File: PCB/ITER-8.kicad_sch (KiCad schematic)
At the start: 23 parts, among them J1 DC-005, J2 Conn_01x16, J3 Conn_01x08, J4 Conn_01x02, SW1 A11JP, SW2 Dual Push Button, U1 W65C02S6TPG-14, U2 AT28C256-15PU, U3 AS6C62256-55PCN, U4 W65C22SxP, U5 SN74HC00N, Y1 ECS-100AX-010

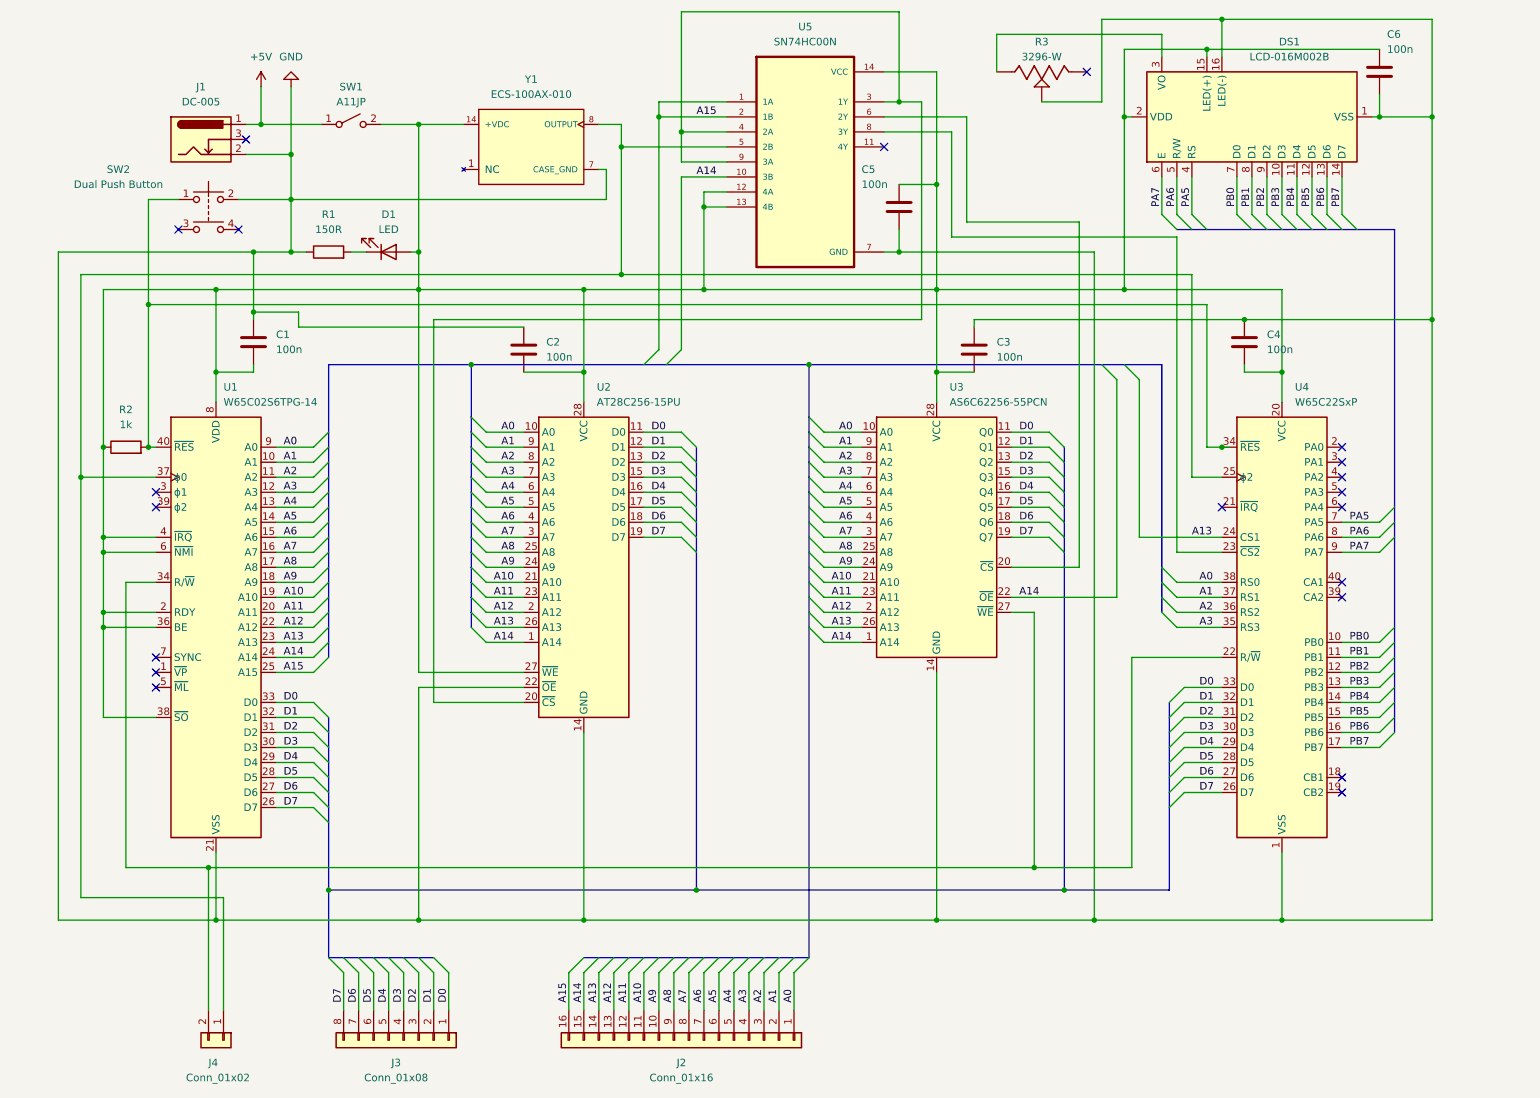
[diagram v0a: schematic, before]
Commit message: 4-bit LCD
LCD in 4-bit mode, including assembly subroutines for timings. New test of the division with remainder.
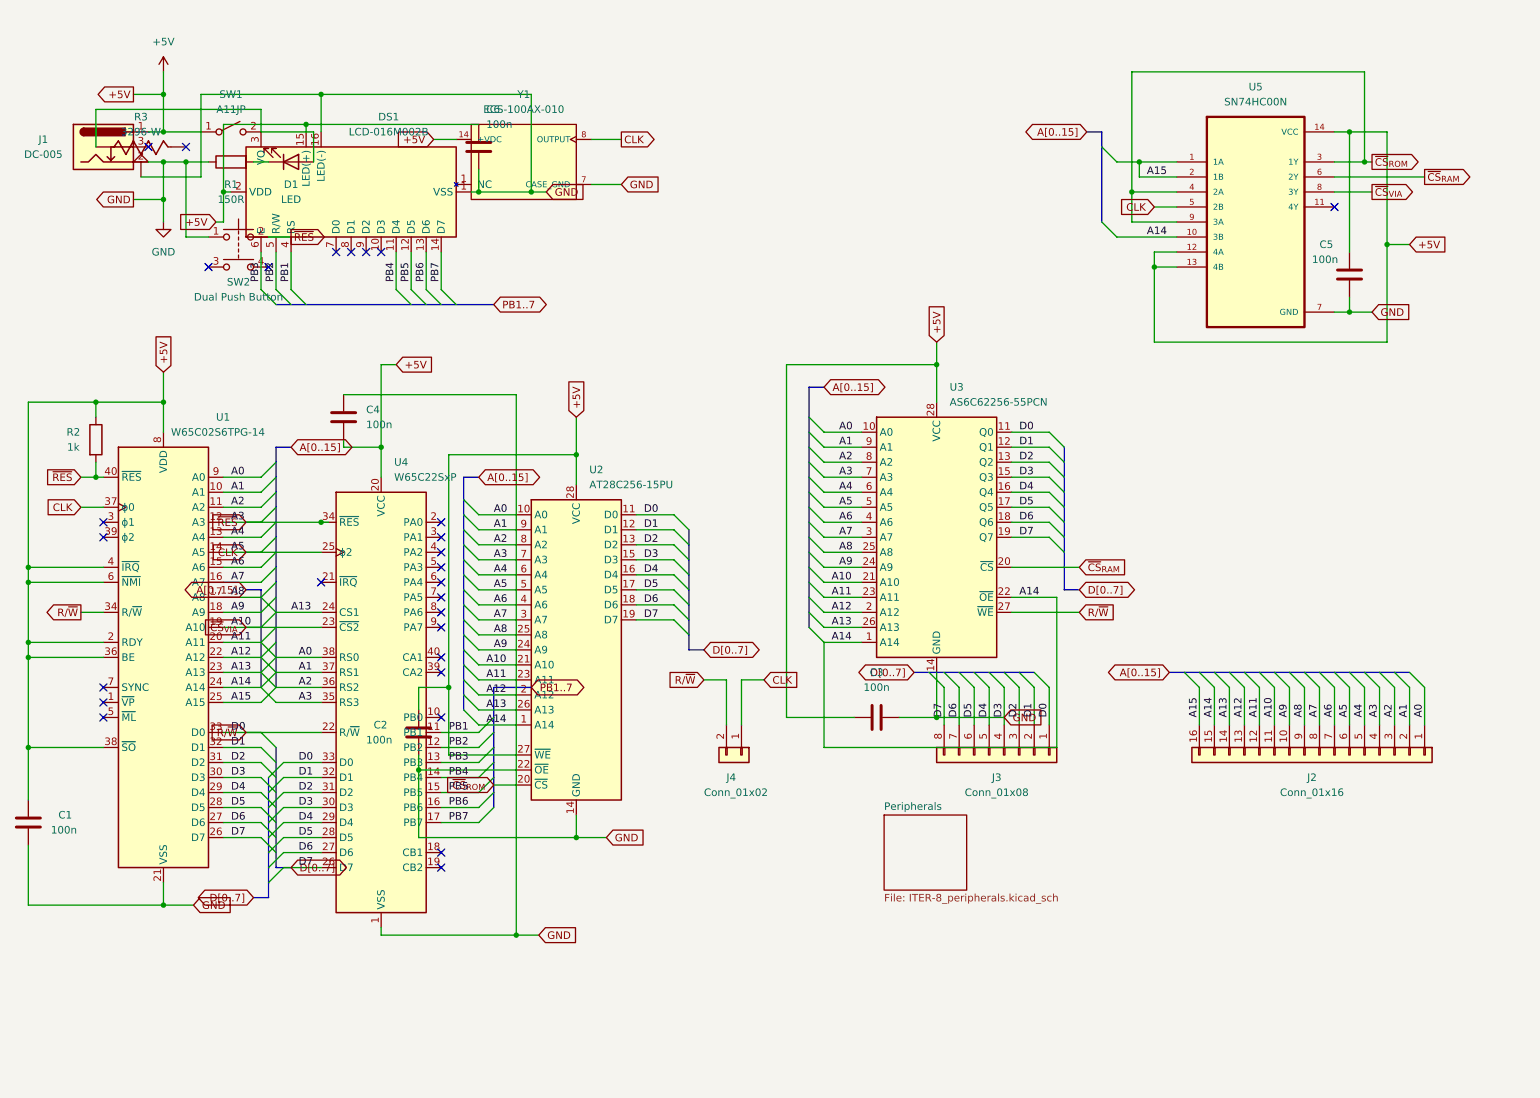
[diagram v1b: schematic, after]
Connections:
- net A10 is gone; now on net ~{CS}_{VIA}: J2.11 (Pin_11), U1.19 (A10), U2.21 (A10), U3.21 (A10)
- net A3 is gone; now on net ~{RES}: J2.4 (Pin_4), U1.12 (A3), U2.7 (A3), U3.7 (A3), U4.35 (RS3)
- net A5 is gone; now on net CLK: J2.6 (Pin_6), U1.14 (A5), U2.5 (A5), U3.5 (A5)
- net D0 is gone; now on net R/~{W}: J3.1 (Pin_1), U1.33 (D0), U2.11 (D0), U3.11 (Q0), U4.33 (D0)
- net D3 is gone; now on net GND: J3.4 (Pin_4), U1.30 (D3), U2.15 (D3), U3.15 (Q3), U4.30 (D3)
- net D4 is gone; now on net GND: J3.5 (Pin_5), U1.29 (D4), U2.16 (D4), U3.16 (Q4), U4.29 (D4)
- net D5 is gone; now on net GND: J3.6 (Pin_6), U1.28 (D5), U2.17 (D5), U3.17 (Q5), U4.28 (D5)
- net D6 is gone; now on net GND: J3.7 (Pin_7), U1.27 (D6), U2.18 (D6), U3.18 (Q6), U4.27 (D6)
- net D7 is gone; now on net GND: J3.8 (Pin_8), U1.26 (D7), U2.19 (D7), U3.19 (Q7), U4.26 (D7)
- net +5V: now also C1.1, C2.1, C3.1, C4.2, C5.1, C6.1, DS1.15 (LED(+)), DS1.2 (VDD), DS1.4 (RS), DS1.5 (R/W), R2.1, U1.2 (RDY), U1.36 (BE), U1.38 (~{SO}), U1.4 (~{IRQ}), U1.6 (~{NMI}), U1.8 (VDD), U2.27 (~{WE}), U2.28 (VCC), U3.28 (VCC), U4.11 (PB1), U4.12 (PB2), U4.20 (VCC), U5.12 (4A), U5.13 (4B), U5.14 (VCC), Y1.14 (+VDC)
- net GND: now also C1.2, C2.2, C3.2, SW2.1; no longer C1.1, C2.1, C3.1, SW2.2
- net PB3: now also DS1.6 (E); no longer DS1.10 (D3)
- net CLK: now reaches J4.1 (Pin_1), U1.37 (ϕ0), U4.25 (ϕ2), U5.5 (2B), Y1.8 (OUTPUT)
- net R/~{W}: now reaches J4.2 (Pin_2), U1.34 (R/~{W}), U3.27 (~{WE}), U4.22 (R/~{W})
- net ~{RES}: now reaches R2.2, U1.40 (~{RES}), U4.34 (~{RES})
- net ~{RES}: now also SW2.2; no longer SW2.1
- net at DS1.3 (VO), R3.1: now also D1.2 (A), SW1.2 (B)
- net ~{CS}_{ROM}: now reaches U2.20 (~{CS}), U5.3 (1Y), U5.4 (2A), U5.9 (3A)
- net ~{CS}_{VIA}: now reaches U4.23 (~{CS2}), U5.8 (3Y)
- net ~{CS}_{RAM}: now reaches U3.20 (~{CS}), U5.6 (2Y)
- net PA5: no longer names the net of U4.7 (PA5)
- net PA5: no longer DS1.4 (RS)
- net PA6: no longer names the net of U4.8 (PA6)
- net PA6: no longer DS1.5 (R/W)
- net PA7: no longer names the net of U4.9 (PA7)
- net PA7: no longer DS1.6 (E)
- net PB0: no longer names the net of U4.10 (PB0)
- net PB0: no longer DS1.7 (D0)
- net PB1: no longer names the net of DS1.8 (D1)
- net PB1: no longer U4.11 (PB1)
- net PB2: no longer names the net of DS1.9 (D2)
- net PB2: no longer U4.12 (PB2)
- no-connect marks 20 -> 28
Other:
- added sheet Peripherals (ITER-8_peripherals.kicad_sch)
- company: (none) -> by Paolo Turri
- title: 6502 Generic Purpose Computer -> ITER-8 - Main
- moved on the sheet: C1, C2, C3, C5, D1, J1, R1, R2, SW1, SW2, U1, U2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

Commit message: Button interrupt
New test to count the number of interrupts from a push button. The power section has been changed to automatically reset the computer.
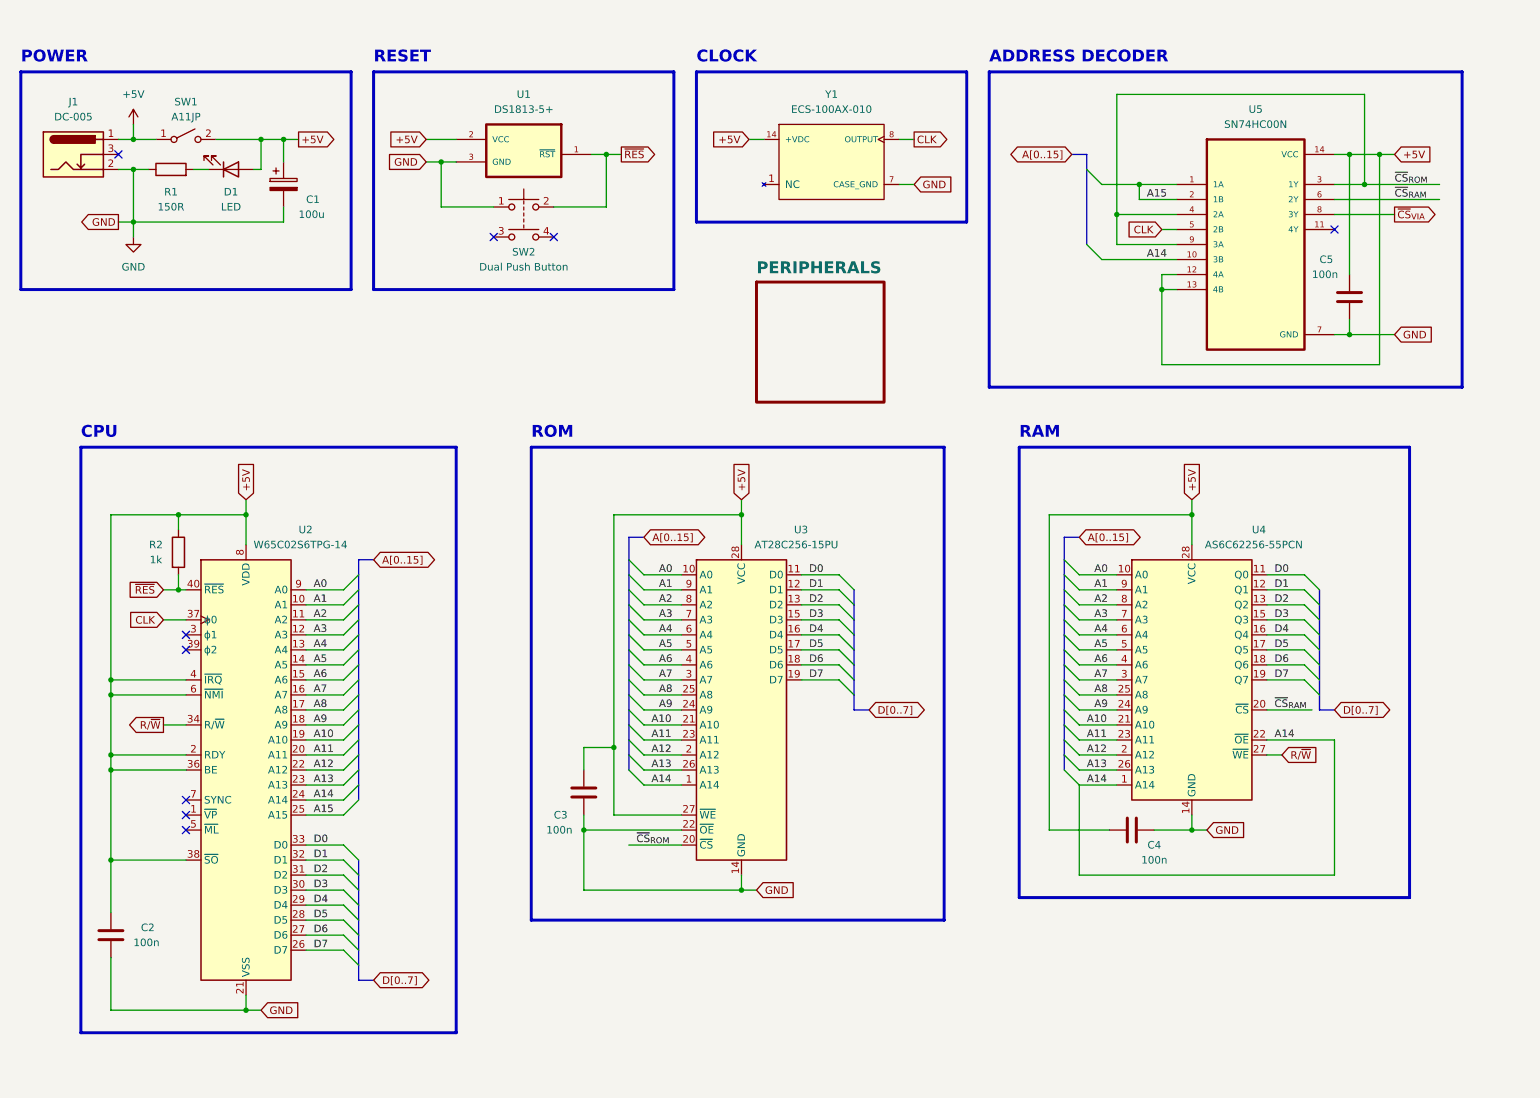
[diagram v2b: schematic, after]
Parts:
- removed C4, C6: 100n, Capacitor_THT:C_Disc_D5.0mm_W2.5mm_P5.00mm, symbol Device:C
- removed DS1: LCD-016M002B, Display:WC1602A, symbol Display_Character:WC1602A
- removed J2: Conn_01x16, Connector_PinSocket_2.54mm:PinSocket_1x16_P2.54mm_Vertical, symbol Connector_Generic:Conn_01x16
- removed J3: Conn_01x08, Connector_PinSocket_2.54mm:PinSocket_1x08_P2.54mm_Vertical, symbol Connector_Generic:Conn_01x08
- removed J4: Conn_01x02, Connector_PinSocket_2.54mm:PinSocket_1x02_P2.54mm_Vertical, symbol Connector_Generic:Conn_01x02
- removed R3: 3296-W, SnapEDA Library:TRIM_3296-W, symbol 3296-W:3296-W
- removed U4: W65C22SxP, Package_DIP:DIP-40_W15.24mm, symbol PCM_65xx-library:W65C22SxP
- added C1: 100u, symbol Device:C_Polarized
- added U1: DS1813-5+, SnapEDA Library:TO92127P495H695-3, symbol DS1813-5:DS1813-5
- renumbered C1 to C2, C2 to C3, C3 to C4, U1 to U2, U2 to U3, U3 to U4
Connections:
- net +5V: now also D1.2 (A), SW1.2 (B), C1.1, U1.2 (VCC)
- net CLK: no longer U2.14 (A5), U3.5 (A5), U4.5 (A5)
- net GND: now also C1.2, U1.3 (GND); no longer U2.26 (D7), U2.27 (D6), U2.28 (D5), U2.29 (D4), U2.30 (D3), U3.15 (D3), U3.16 (D4), U3.17 (D5), U3.18 (D6), U3.19 (D7), U4.15 (Q3), U4.16 (Q4), U4.17 (Q5), U4.18 (Q6), U4.19 (Q7)
- net R/~{W}: no longer U2.33 (D0), U3.11 (D0), U4.11 (Q0)
- net ~{CS}_{VIA}: no longer U2.19 (A10), U3.21 (A10), U4.21 (A10)
- net ~{RES}: now also U1.1 (~{RST}); no longer U2.12 (A3), U3.7 (A3), U4.7 (A3)
- new net A10: U2.19 (A10), U3.21 (A10), U4.21 (A10)
- new net A3: U2.12 (A3), U3.7 (A3), U4.7 (A3)
- new net A5: U2.14 (A5), U3.5 (A5), U4.5 (A5)
- new net D0: U2.33 (D0), U3.11 (D0), U4.11 (Q0)
- new net D3: U2.30 (D3), U3.15 (D3), U4.15 (Q3)
- new net D4: U2.29 (D4), U3.16 (D4), U4.16 (Q4)
- new net D5: U2.28 (D5), U3.17 (D5), U4.17 (Q5)
- new net D6: U2.27 (D6), U3.18 (D6), U4.18 (Q6)
- new net D7: U2.26 (D7), U3.19 (D7), U4.19 (Q7)
- no-connect marks 28 -> 9
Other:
- sheet Peripherals renamed PERIPHERALS
- note added: "ADDRESS DECODER"
- note added: "CLOCK"
- note added: "CPU"
- note added: "POWER"
- note added: "RAM"
- note added: "RESET"
- note added: "ROM"
- moved on the sheet: C2, C3, C4, C5, D1, J1, R1, R2, SW1, SW2, U2, U3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
